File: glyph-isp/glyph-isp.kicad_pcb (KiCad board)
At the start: 2 copper layers, 29 x 10 mm, 17 parts, among them J0 ISP, J1 Target ISP, J2 USB-Micro, U0 ATmega16U4-MU, Y1 16MHz

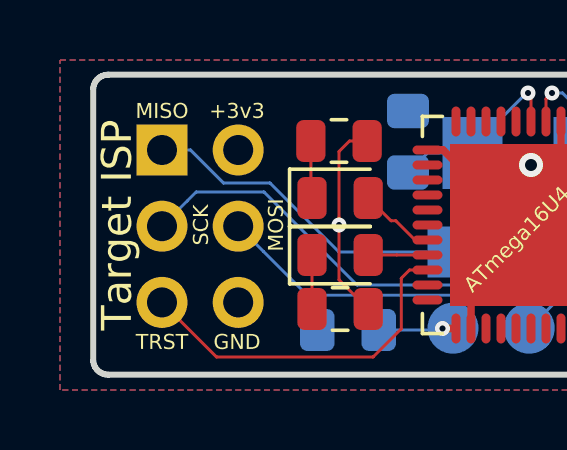
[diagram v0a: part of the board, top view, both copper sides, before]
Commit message: capacitor values consistent
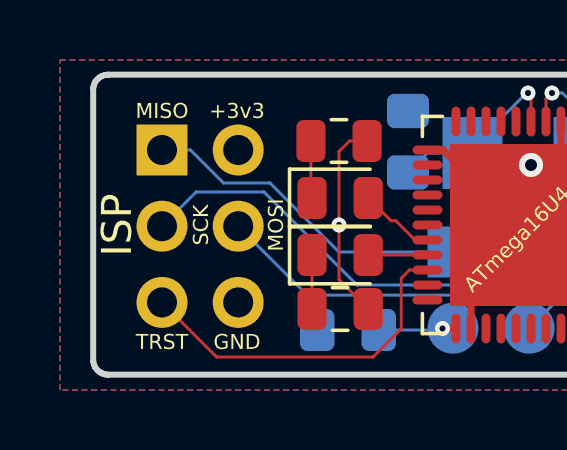
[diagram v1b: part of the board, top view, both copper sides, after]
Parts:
- C0: value 104 -> 0.1uF
- J1: value Target ISP -> ISP
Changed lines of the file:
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@@
     (35 F.Paste user hide)
     (36 B.SilkS user)
-    (37 F.SilkS user hide)
+    (37 F.SilkS user)
     (38 B.Mask user hide)
     (39 F.Mask user hide)
@@
     (46 B.CrtYd user hide)
     (47 F.CrtYd user hide)
-    (48 B.Fab user)
+    (48 B.Fab user hide)
     (49 F.Fab user hide)
   )
@@
       (effects (font (size 1 1) (thickness 0.15)))
     )
-    (fp_text value "Target ISP" (at -1.5 2.5 90) (layer F.SilkS)
+    (fp_text value ISP (at -1.5 2.5 90) (layer F.SilkS)
       (effects (font (size 1 1) (thickness 0.15)))
     )
@@
       (effects (font (size 1 1) (thickness 0.15)) (justify mirror))
     )
-    (fp_text value 104 (at 0 -1.65 270) (layer B.SilkS)
+    (fp_text value 0.1uF (at 0 -1.65 270) (layer B.SilkS)
       (effects (font (size 1 1) (thickness 0.15)) (justify mirror))
     )
@@
   (gr_line (start 127.5 72.5) (end 127.4005 72.53229) (layer Edge.Cuts) (width 0.2))
   (via (at 135.3 77.5) (size 0.5) (drill 0.2) (layers F.Cu B.Cu) (net 1))
-  (via (at 149.7 73.7) (size 0.5) (drill 0.2) (layers F.Cu B.Cu) (net 2))
-  (via (at 138.75 80.95) (size 0.5) (drill 0.2) (layers F.Cu B.Cu) (net 2))
   (via (at 141.7 75.5) (size 0.8) (drill 0.4) (layers F.Cu B.Cu) (net 1))
   (segment (start 139.7 79.5) (end 141.7 77.5) (width 0.25) (layer F.Cu) (net 1))
@@
   (segment (start 154.55 76.5) (end 154.55 74) (width 0.25) (layer F.Cu) (net 1))
   (segment (start 154.55 76.5) (end 154.55 78.5) (width 0.25) (layer F.Cu) (net 1))
+  (via (at 149.7 73.7) (size 0.5) (drill 0.2) (layers F.Cu B.Cu) (net 2))
+  (via (at 138.75 80.95) (size 0.5) (drill 0.2) (layers F.Cu B.Cu) (net 2))
   (segment (start 139.2 80.95) (end 138.75 80.95) (width 0.25) (layer F.Cu) (net 2))
   (segment (start 136.625 81) (end 136.9 81) (width 0.25) (layer B.Cu) (net 2))

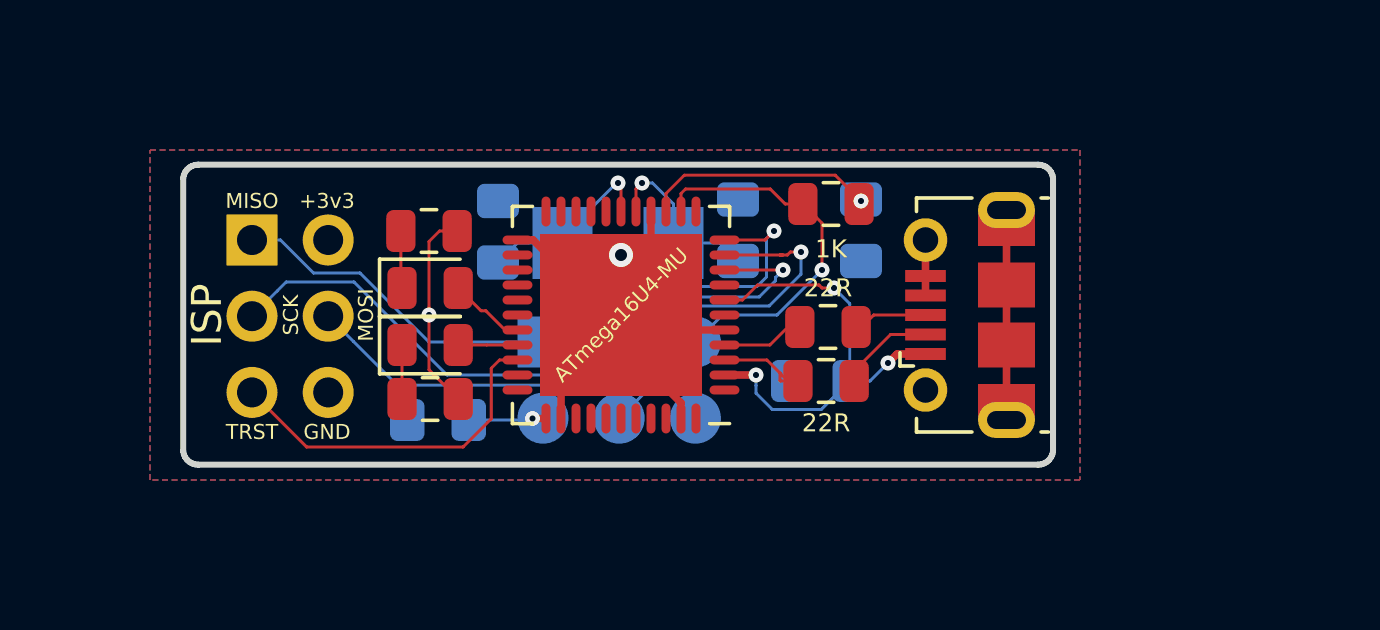
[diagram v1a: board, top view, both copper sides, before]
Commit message: reworked ISP size
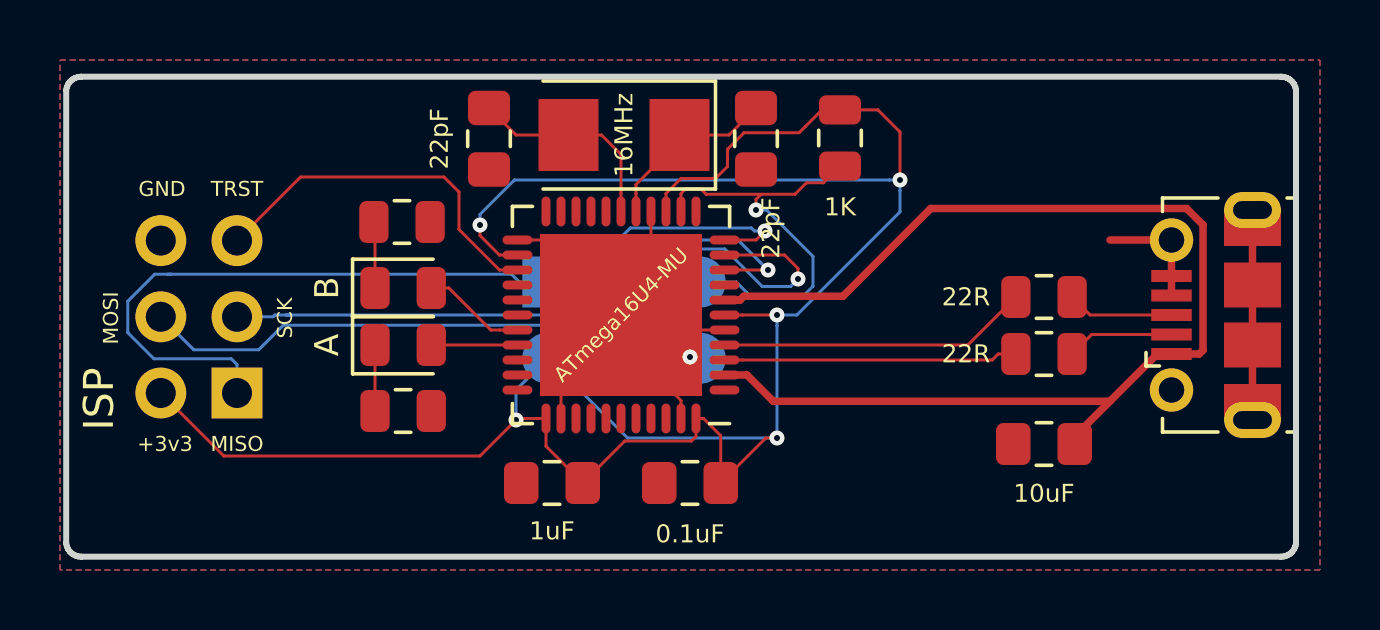
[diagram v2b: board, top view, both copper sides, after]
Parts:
- C0, C1, C2, C3, C4, Y1: moved to F.Cu
- moved C0 10.2 mm to (144.0, 83.1), turned to 180 degrees
- moved J2 8.20 mm to (162.4, 77.5)
- moved C4 7.79 mm to (155.8, 81.8)
- moved R5 7.32 mm to (155.8, 78.8)
- moved R4 7.27 mm to (155.8, 76.9)
- moved J1 5.12 mm to (128.9, 80.1), turned to 180 degrees
- moved C3 4.34 mm to (139.4, 83.1)
- moved Y1 3.61 mm to (141.8, 71.5)
- moved C1 3.11 mm to (137.3, 71.6), turned to 270 degrees
- moved C2 3.11 mm to (146.2, 71.6), turned to 270 degrees
- moved R1 2.22 mm to (149.0, 71.6), turned to 270 degrees
- moved J0 2.01 mm to (139.3, 76.4)
- moved R3 0.98 mm to (134.4, 80.7)
- moved R2 0.95 mm to (134.4, 74.4)
- moved D1 0.90 mm to (134.4, 76.6)
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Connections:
- U0 pad 25: (no net) -> TARGET_RESET
- U0 pad 31: TARGET_RESET -> (no net)
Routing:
- net +3V3: track 10.9 -> 78.6 mm, vias 2 -> 5
- net VBUS: track 15.5 -> 40.6 mm, vias 3 -> 0
- net D+: track 2.76 -> 10.4 mm
- net MISO: track 23.6 -> 30.2 mm
- net D-: track 3.26 -> 9.80 mm
- net GND: track 36.8 -> 31.5 mm, vias 2 -> 1
- net MOSI: track 24.4 -> 28.6 mm
- net SCK: track 22.9 -> 20.8 mm
- net RESET: track 12.6 -> 14.6 mm
- net TARGET_RESET: track 11.8 -> 13.0 mm
- net LED2: track 1.97 -> 2.88 mm
- net LED1: track 2.55 -> 3.45 mm
- net Net-(C1-Pad1): track 6.21 -> 6.94 mm, vias 1 -> 0
- net Net-(J2-Pad3): track 2.88 -> 3.56 mm
- net Net-(C2-Pad1): vias 1 -> 0
- added copper zone on F.Cu, net GND
- removed copper zone on F.Cu, net +3V3
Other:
- board size 29 x 10 mm -> 41 x 16 mm
- board text added: "A"
- board text added: "B"

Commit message: added logo
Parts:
- added HAT: , HAT, F.Cu at (148.0, 80.0)
